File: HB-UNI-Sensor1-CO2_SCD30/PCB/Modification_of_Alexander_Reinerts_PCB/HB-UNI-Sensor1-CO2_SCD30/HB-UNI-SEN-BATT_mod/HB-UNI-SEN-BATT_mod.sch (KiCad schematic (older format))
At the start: 35 parts, among them J10 Conn_01x02-conn, J11 Conn_01x04-conn, J12 Conn_01x04-conn, J13 Conn_01x04-conn, J14 Conn_01x04-conn, J4 Conn_01x02-conn, J5 GS2-conn, J6 Conn_01x04-conn, J7 Conn_01x02-conn, J8 Conn_01x02-conn, J9 Conn_01x02-conn, Q1 BC327, SW2 SW_DIP_x01-switches, U1 CC1101-RESCUE-HB-UNI-SEN-BATT, U2 ArduinoProMini

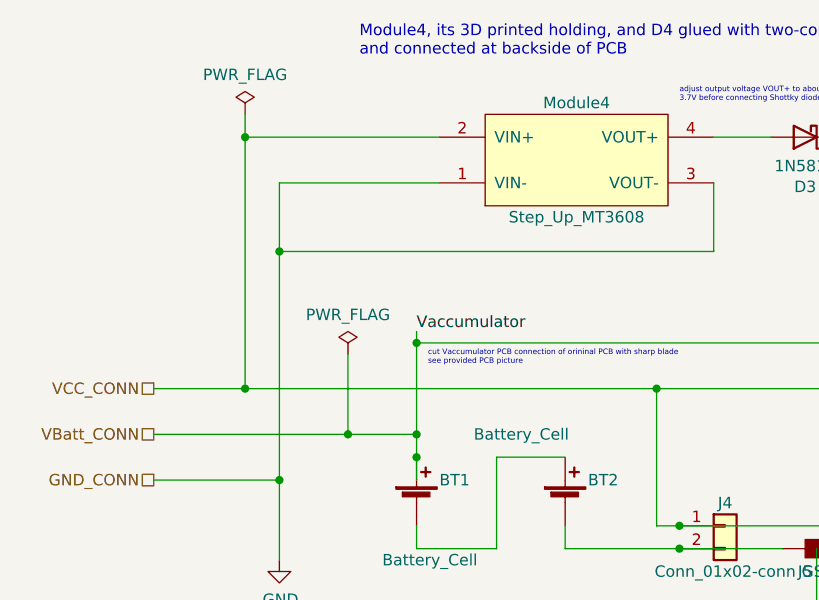
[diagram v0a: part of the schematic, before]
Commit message: Fixed schematic mistake
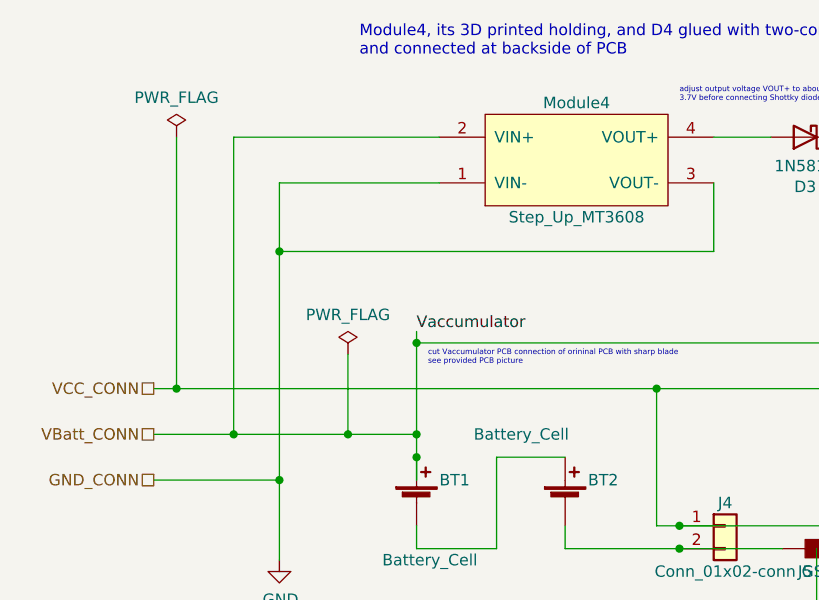
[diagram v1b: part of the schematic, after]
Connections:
- wire segments 185 -> 186
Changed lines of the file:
@@
 Wire Wire Line
 	2400 6700 2400 6600
-Wire Wire Line
-	1750 2250 2150 2250
 Connection ~ 2400 6600
 Wire Wire Line
@@
 Wire Wire Line
 	2300 1350 2300 1650
-Connection ~ 2150 2250
-Wire Wire Line
-	2150 2250 3950 2250
 Wire Wire Line
 	4200 1150 4450 1150
@@
 	2600 2450 2900 2450
 Wire Wire Line
-	1750 2450 2600 2450
-Wire Wire Line
 	2600 2100 2600 2450
 $Comp
@@
 Connection ~ 8350 1500
 Connection ~ 8750 1500
-$Comp
-L power:PWR_FLAG #FLG08
-U 1 1 5F680073
-P 2150 1050
-F 0 "#FLG08" H 2150 1125 50  0001 C CNN
-F 1 "PWR_FLAG" H 2150 1223 50  0000 C CNN
-F 2 "" H 2150 1050 50  0001 C CNN
-F 3 "~" H 2150 1050 50  0001 C CNN
-	1    2150 1050
-	1    0    0    -1
-$EndComp
-Wire Wire Line
-	2150 1050 2150 1150
-Wire Wire Line
-	3000 1150 2150 1150
-Connection ~ 2150 1150
-Wire Wire Line
-	2150 1150 2150 2250
 Wire Wire Line
 	3000 1350 2300 1350
@@
 Connection ~ 4050 2850
 Connection ~ 5450 2850
+Wire Wire Line
+	3000 1150 2100 1150
+$Comp
+L power:PWR_FLAG #FLG0101
+U 1 1 5F50FD78
+P 1850 1150
+F 0 "#FLG0101" H 1850 1225 50  0001 C CNN
+F 1 "PWR_FLAG" H 1850 1323 50  0000 C CNN
+F 2 "" H 1850 1150 50  0001 C CNN
+F 3 "~" H 1850 1150 50  0001 C CNN
+	1    1850 1150
+	1    0    0    -1
+$EndComp
+Wire Wire Line
+	1750 2450 2100 2450
+Wire Wire Line
+	1750 2250 1850 2250
+Wire Wire Line
+	2100 1150 2100 2450
+Connection ~ 2100 2450
+Wire Wire Line
+	2100 2450 2600 2450
+Wire Wire Line
+	1850 1150 1850 2250
+Connection ~ 1850 2250
+Wire Wire Line
+	1850 2250 3950 2250
 $EndSCHEMATC

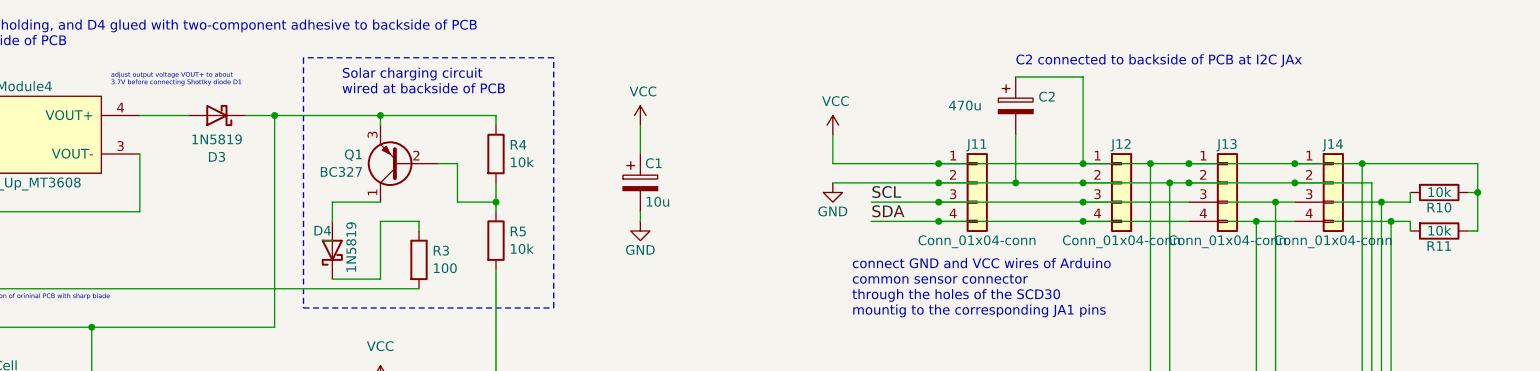
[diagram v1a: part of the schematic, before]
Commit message: Reduced charge current of NiMH charging module, added and deleted a capacitor in schematic sheet 'Power Supply'
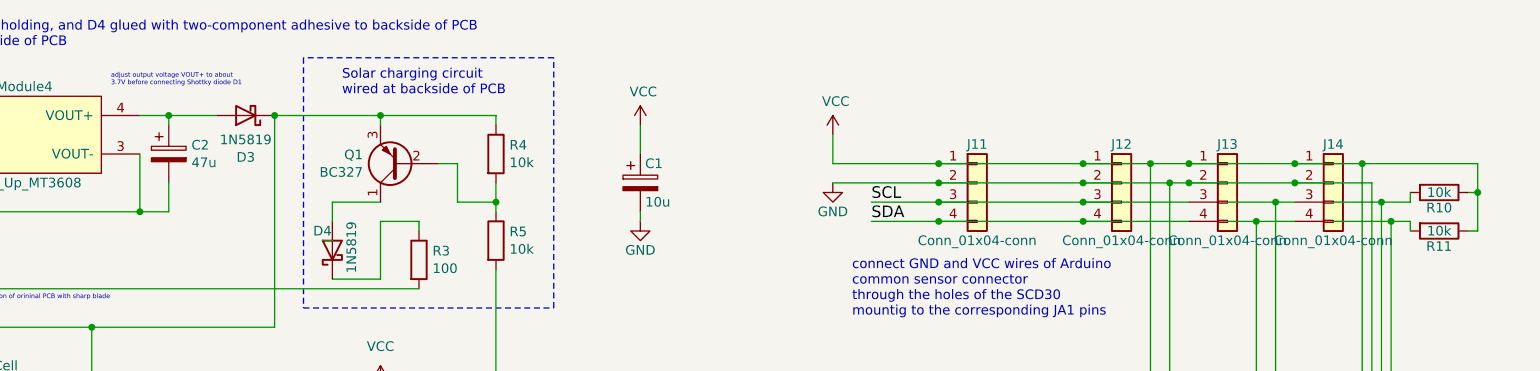
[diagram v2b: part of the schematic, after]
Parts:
- C2: value 470u -> 47u
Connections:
- wire segments 186 -> 185
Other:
- note removed: "C2 connected to backside of PCB at I2C JAx"
- moved on the sheet: D3
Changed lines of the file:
@@
 	2400 6600 2400 6500
-$Comp
-L Device:CP C2
-U 1 1 5F3BD123
-P 8750 1100
-F 0 "C2" H 8868 1146 50  0000 L CNN
-F 1 "470u" H 8400 1100 50  0000 L CNN
-F 2 "" H 8788 950 50  0001 C CNN
-F 3 "~" H 8750 1100 50  0001 C CNN
-	1    8750 1100
-	1    0    0    -1
-$EndComp
-Wire Wire Line
-	8750 1250 8750 1500
-Wire Wire Line
-	8750 950  9100 950
-Text Notes 8750 900  0    50   ~ 0
-C2 connected to backside of PCB at I2C JAx
 $Comp
 L HB-UNI-Sensor1-CO2_SCD30:Step_Up_MT3608 Module?
@@
 	1    0    0    -1
 $EndComp
-$Comp
-L Diode:1N5819 D3
-U 1 1 5F3959ED
-P 4600 1150
-F 0 "D3" H 4600 1367 50  0000 C CNN
-F 1 "1N5819" H 4600 1276 50  0000 C CNN
-F 2 "Diode_THT:D_DO-41_SOD81_P10.16mm_Horizontal" H 4600 975 50  0001 C CNN
-F 3 "http://www.vishay.com/docs/88525/1n5817.pdf" H 4600 1150 50  0001 C CNN
-	1    4600 1150
-	-1   0    0    1
-$EndComp
 Connection ~ 2900 2550
 Wire Wire Line
@@
 	2300 1350 2300 1650
 Wire Wire Line
-	4200 1150 4450 1150
-Wire Wire Line
-	4750 1150 4900 1150
-Wire Wire Line
-	4900 1150 4900 2250
+	4200 1150 4350 1150
 Wire Wire Line
 	4900 2250 3950 2250
@@
 	2900 2050 2900 2450
 Connection ~ 2900 2450
-Connection ~ 4900 1150
 Connection ~ 2600 2450
 Wire Wire Line
@@
 Wire Wire Line
 	8350 1700 8000 1700
-Wire Wire Line
-	9100 950  9100 1400
 Connection ~ 9100 1400
 Wire Wire Line
 	9100 1400 9450 1400
-Wire Wire Line
-	9100 1500 8750 1500
 $Comp
 L HB-UNI-SEN-BATT-rescue:Conn_01x04-conn J14
@@
 $EndComp
 Wire Wire Line
-	4900 1150 5450 1150
-Wire Wire Line
 	6050 1500 6050 1600
 Wire Wire Line
 	5450 1200 5450 1150
-Connection ~ 5450 1150
 Wire Wire Line
 	5450 1150 6050 1150
@@
 	8350 1400 9100 1400
 Connection ~ 8350 1400
-Wire Wire Line
-	8350 1500 8750 1500
 Connection ~ 8350 1500
-Connection ~ 8750 1500
 Wire Wire Line
 	3000 1350 2300 1350
@@
 Wire Wire Line
 	1850 2250 3950 2250
+Wire Wire Line
+	8350 1500 9100 1500
+$Comp
+L Device:CP C2
+U 1 1 5F56C474
+P 4350 1350
+F 0 "C2" H 4468 1396 50  0000 L CNN
+F 1 "47u" H 4468 1305 50  0000 L CNN
+F 2 "" H 4388 1200 50  0001 C CNN
+F 3 "~" H 4350 1350 50  0001 C CNN
+	1    4350 1350
+	1    0    0    -1
+$EndComp
+Connection ~ 5450 1150
+Wire Wire Line
+	4900 1150 5450 1150
+Connection ~ 4900 1150
+Wire Wire Line
+	4900 1150 4900 2250
+$Comp
+L Diode:1N5819 D3
+U 1 1 5F3959ED
+P 4750 1150
+F 0 "D3" H 4750 1367 50  0000 C CNN
+F 1 "1N5819" H 4750 1276 50  0000 C CNN
+F 2 "Diode_THT:D_DO-41_SOD81_P10.16mm_Horizontal" H 4750 975 50  0001 C CNN
+F 3 "http://www.vishay.com/docs/88525/1n5817.pdf" H 4750 1150 50  0001 C CNN
+	1    4750 1150
+	-1   0    0    1
+$EndComp
+Wire Wire Line
+	4350 1200 4350 1150
+Connection ~ 4350 1150
+Wire Wire Line
+	4350 1150 4600 1150
+Wire Wire Line
+	4350 1500 4350 1650
+Wire Wire Line
+	4350 1650 4200 1650
+Connection ~ 4200 1650
 $EndSCHEMATC
